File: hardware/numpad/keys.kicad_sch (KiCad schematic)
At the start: 38 parts

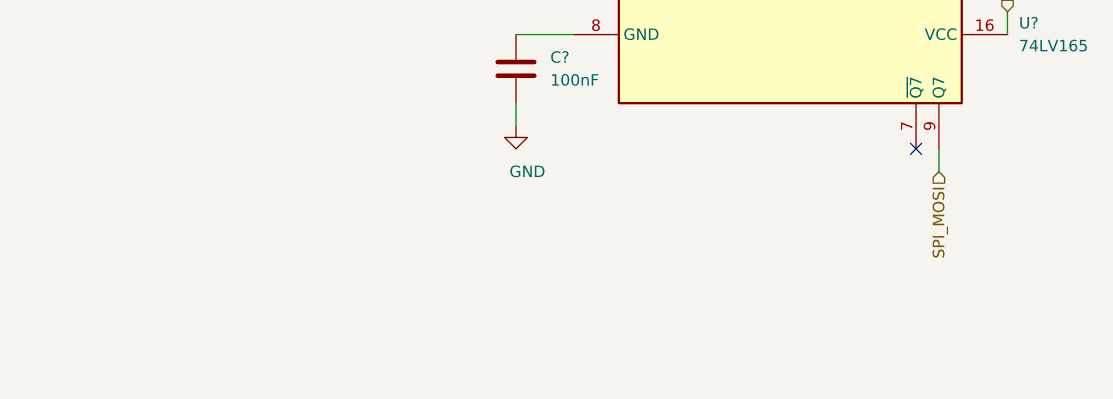
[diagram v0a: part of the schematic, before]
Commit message: Add the missing MISO to the connector
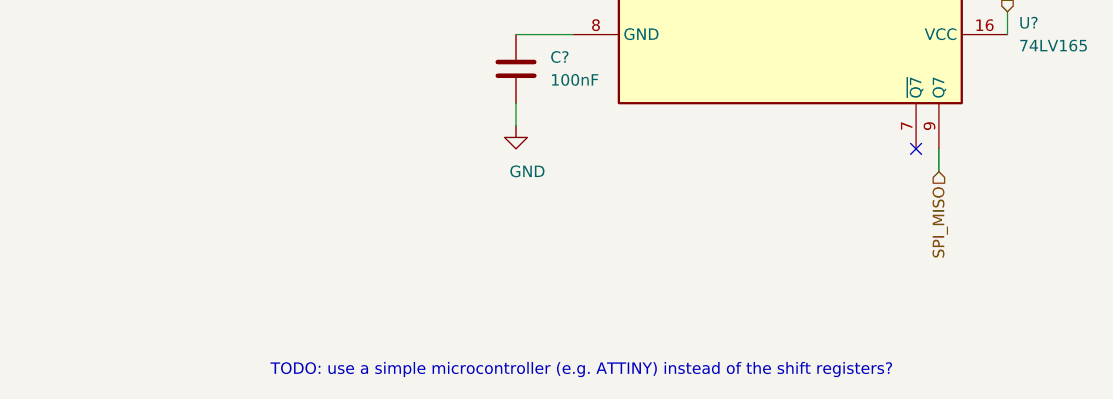
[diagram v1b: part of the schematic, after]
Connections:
- net SPI_MOSI: no longer U?.9 (Q7)
- new net SPI_MISO: U?.9 (Q7)
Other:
- note added: "TODO: use a simple microcontroller (e.g. ATTINY) instead of the shift registers?"
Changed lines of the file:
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@@
   (junction (at 158.75 101.6) (diameter 1.016) (color 0 0 0 0))
   (junction (at 158.75 152.4) (diameter 1.016) (color 0 0 0 0))
+  (no_connect (at 120.65 231.14))
+  (no_connect (at 107.95 205.74))
   (no_connect (at 110.49 205.74))
   (no_connect (at 105.41 205.74))
+  (no_connect (at 123.19 205.74))
   (no_connect (at 67.31 73.66))
-  (no_connect (at 123.19 205.74))
   (no_connect (at 102.87 205.74))
-  (no_connect (at 120.65 231.14))
-  (no_connect (at 107.95 205.74))
   (wire (pts (xy 31.75 55.88) (xy 34.29 55.88))
     (stroke (width 0) (type solid) (color 0 0 0 0))
@@
     (effects (font (size 1.27 1.27)) (justify left bottom))
   )
+  (text "TODO: use a simple microcontroller (e.g. ATTINY) instead of the shift registers?"
+    (at 118.11 256.54 0)
+    (effects (font (size 1.27 1.27)) (justify right bottom))
+  )
   (hierarchical_label "SPI_SCK" (shape input) (at 31.75 55.88 180)
     (effects (font (size 1.27 1.27)) (justify right))
@@
     (effects (font (size 1.27 1.27)) (justify left))
   )
-  (hierarchical_label "SPI_MOSI" (shape input) (at 123.19 233.68 270)
+  (hierarchical_label "SPI_MISO" (shape input) (at 123.19 233.68 270)
     (effects (font (size 1.27 1.27)) (justify right))
   )

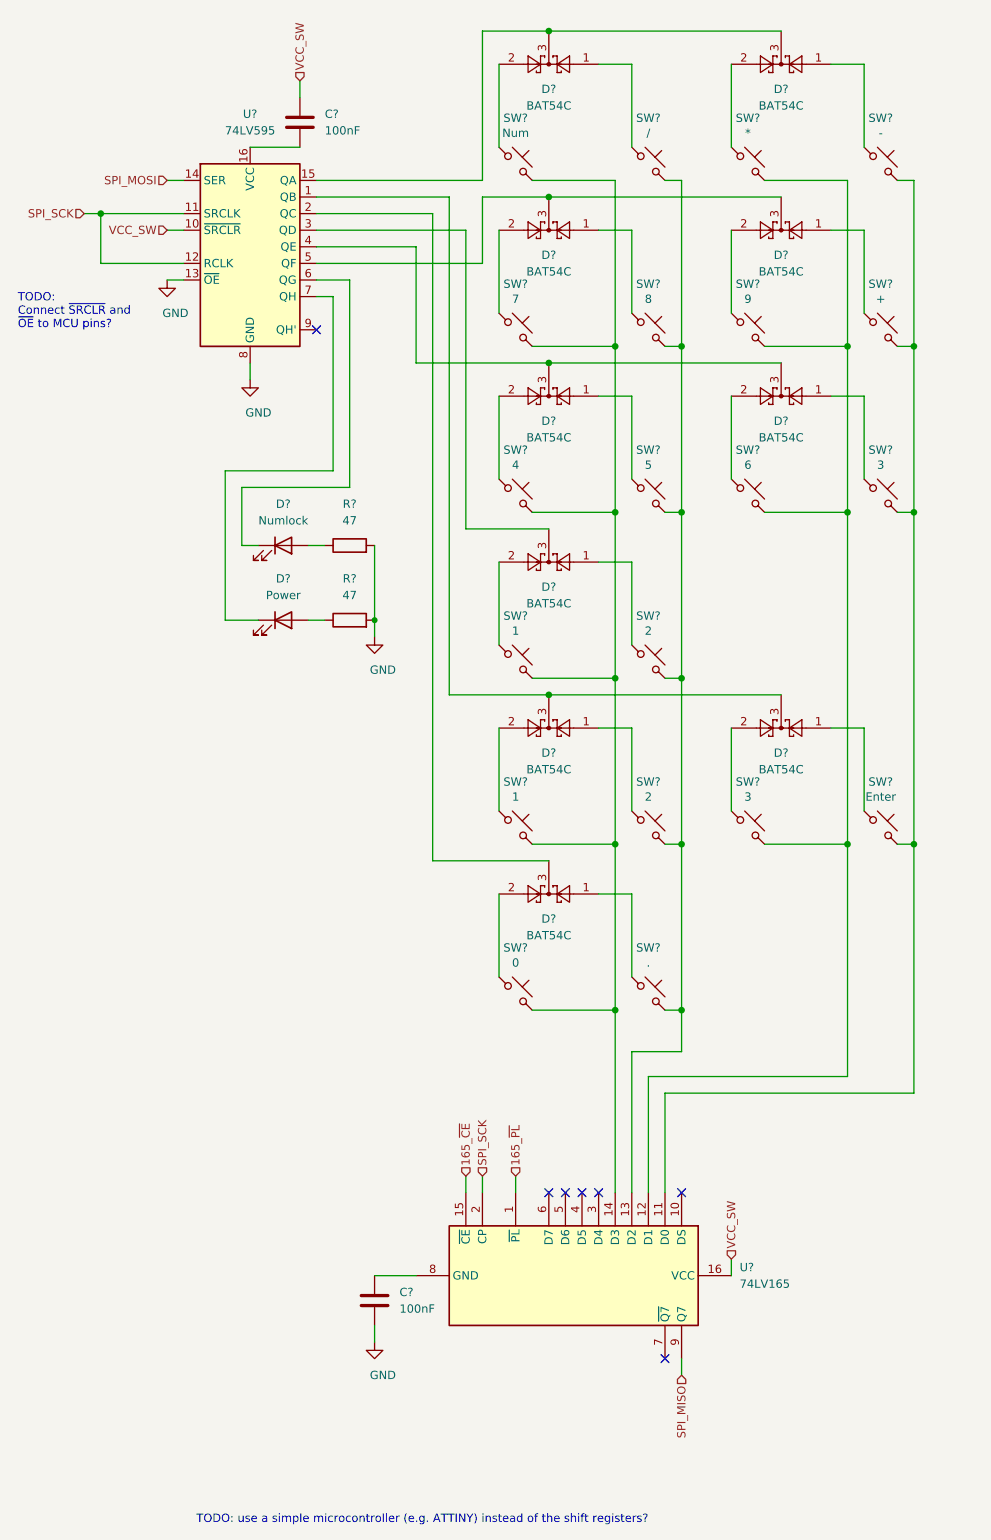
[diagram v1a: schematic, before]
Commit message: WIP: numpad with an ATtiny
As the newer versions of the ATtiny cannot be programmed using an
In-Circuit-Programmer based on SPI this variant is not pursued further.
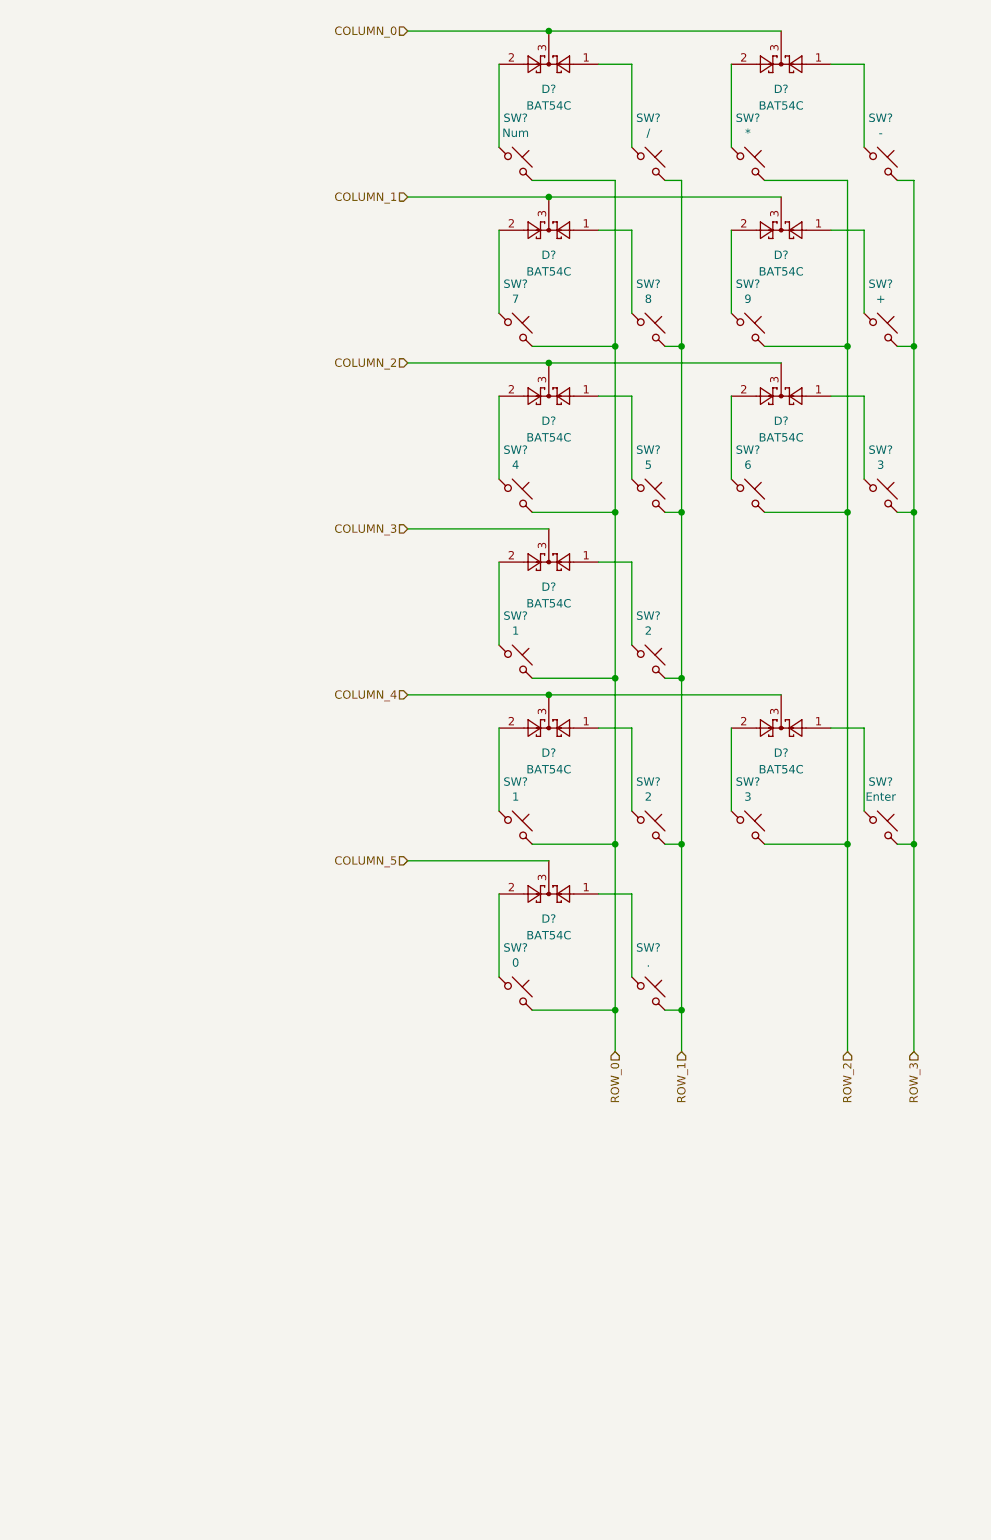
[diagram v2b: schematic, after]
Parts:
- removed C? (x2): 100nF, symbol Device:C
- removed D?: Numlock, symbol Device:LED
- removed D?: Power, symbol Device:LED
- removed R? (x2): 47, symbol Device:R
- removed U?: 74LV595, Package_SO:TSSOP-16_4.4x5mm_P0.65mm, symbol 74xx:74HC595
- removed U?: 74LV165, Package_SO:TSSOP-16_4.4x5mm_P0.65mm, symbol 74xx:74LS165
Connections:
- net ROW_3: now reaches SW?.2, SW?.2, SW?.2, SW?.2
- net ROW_0: now reaches SW?.2, SW?.2, SW?.2, SW?.2, SW?.2, SW?.2
- net COLUMN_0: now reaches D?.3, D?.3
- net COLUMN_2: now reaches D?.3, D?.3
- net COLUMN_3: now reaches D?.3
- net COLUMN_4: now reaches D?.3, D?.3
- net ROW_1: now reaches SW?.2, SW?.2, SW?.2, SW?.2, SW?.2, SW?.2
- net ROW_2: now reaches SW?.2, SW?.2, SW?.2, SW?.2
- net COLUMN_1: now reaches D?.3, D?.3
- net COLUMN_5: now reaches D?.3
- no-connect marks 7 -> 0
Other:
- note removed: "TODO: Connect ~SRCLR and ~OE to MCU pins?"
- note removed: "TODO: use a simple microcontroller (e.g. ATTINY) instead of the shift registers?"

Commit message: Add first rough version of the numpad PCB
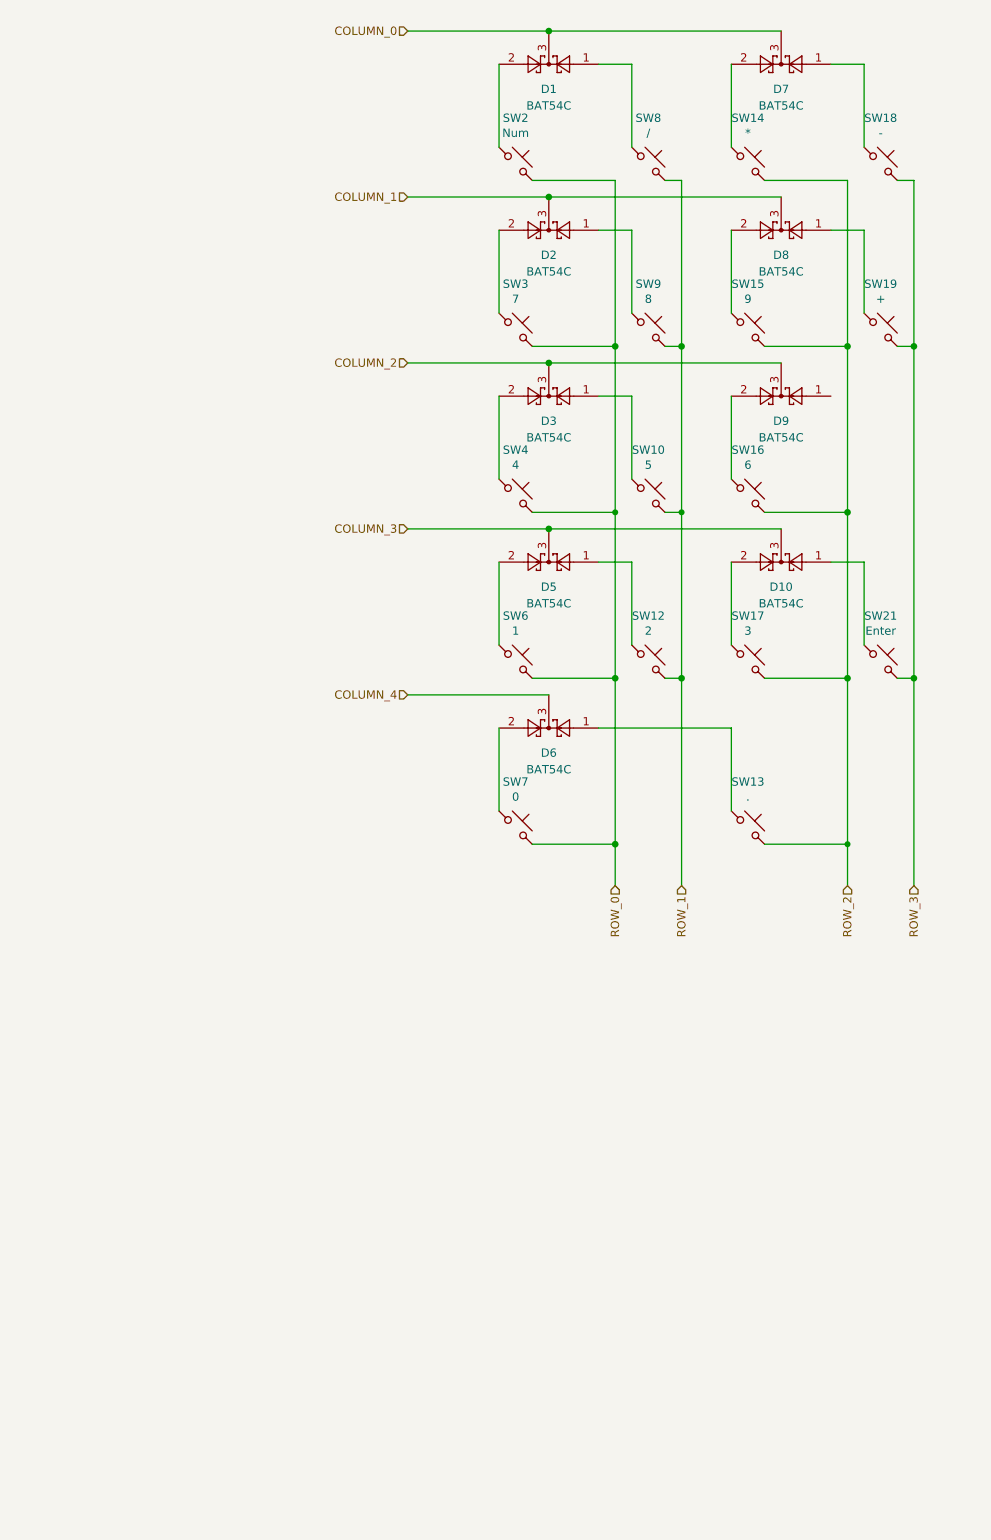
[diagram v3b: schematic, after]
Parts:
- removed D?: BAT54C, Package_TO_SOT_SMD:SOT-23, symbol Diode:BAT54C
- removed SW?: 2, footprints:SW_Cherry_MX_1.00u_PCB, symbol Switch:SW_Push_45deg
- removed SW?: 1, footprints:SW_Cherry_MX_1.75u_PCB, symbol Switch:SW_Push_45deg
- removed SW?: 3, footprints:SW_Cherry_MX_1.00u_PCB, symbol Switch:SW_Push_45deg
- SW13, SW6: renamed from SW?; footprint footprints:SW_Cherry_MX_1.25u_PCB -> footprints:SW_Cherry_MX_1.00u_PCB
- SW19, SW21: renamed from SW?; footprint footprints:SW_Cherry_MX_1.00u_PCB -> footprints:SW_Cherry_MX_2.00u_PCB
- SW4: renamed from SW?; footprint footprints:SW_Cherry_MX_1.50u_PCB -> footprints:SW_Cherry_MX_1.00u_PCB
- SW7: renamed from SW?; footprint footprints:SW_Cherry_MX_1.25u_PCB -> footprints:SW_Cherry_MX_2.00u_PCB
- gave numbers to parts that had none: 20
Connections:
- net COLUMN_5 is gone; now on net COLUMN_4: D6.3
- net COLUMN_3: now also D10.3, D5.3
- net COLUMN_4: no longer D10.3, D5.3
- net ROW_1: no longer SW13.2
- net ROW_2: now also SW13.2
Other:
- moved on the sheet: D10, D5, D6, SW12, SW13, SW17, SW21, SW6, SW7

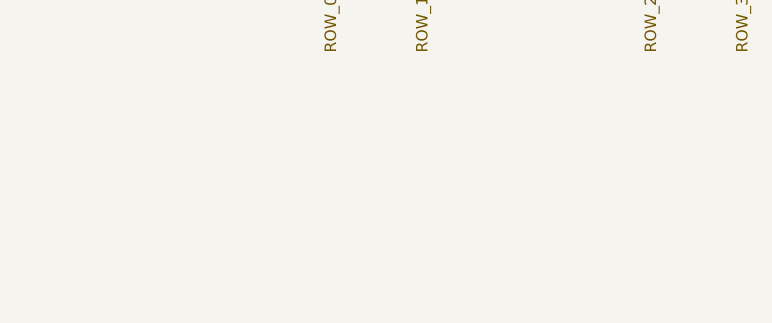
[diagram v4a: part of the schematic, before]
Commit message: Add pull-up resistors to the key matrix
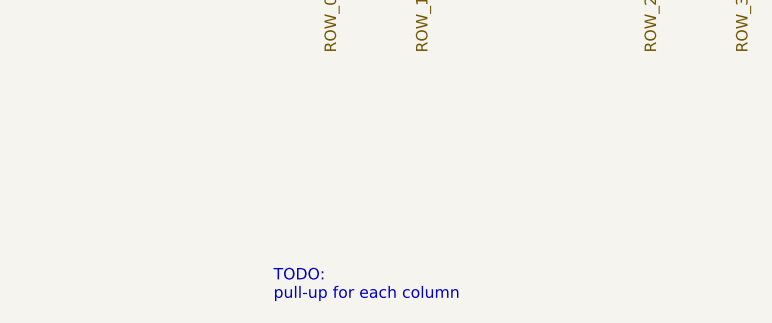
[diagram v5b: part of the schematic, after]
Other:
- note added: "TODO: pull-up for each column"
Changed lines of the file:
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@@
     (stroke (width 0) (type solid) (color 0 0 0 0))
+  )
+  (text "TODO:\npull-up for each column" (at 106.68 194.31 0)
+    (effects (font (size 1.27 1.27)) (justify left bottom))
   )
   (hierarchical_label "COLUMN_0" (shape input) (at 81.28 27.94 180)

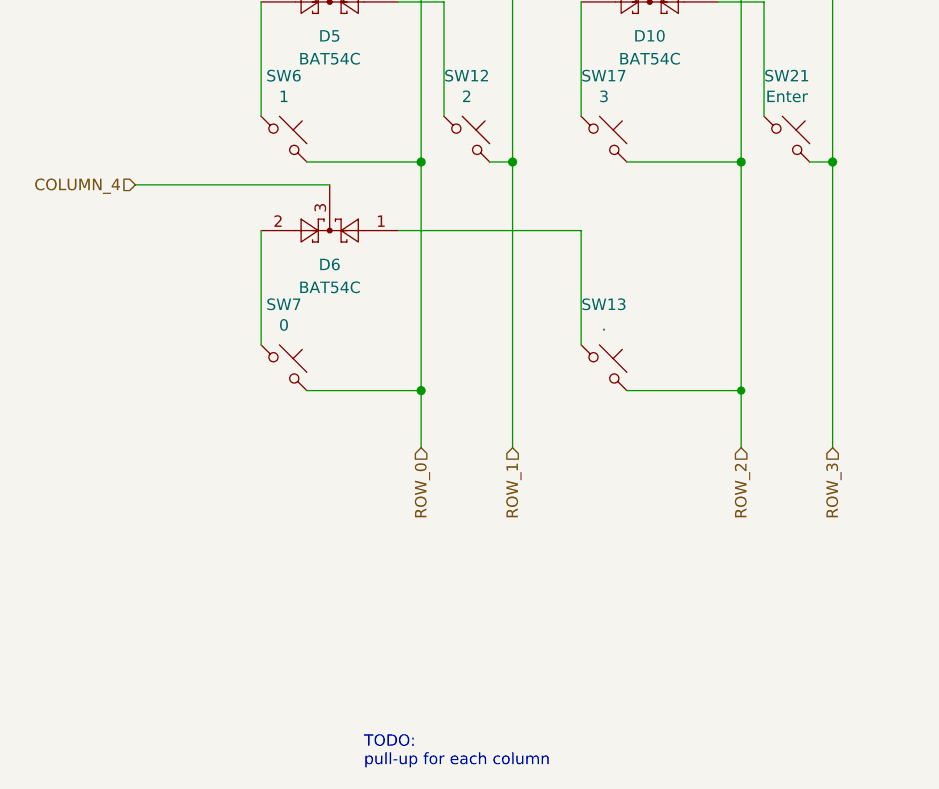
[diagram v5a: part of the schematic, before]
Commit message: Numpad: add pullup resistors to the key matrix
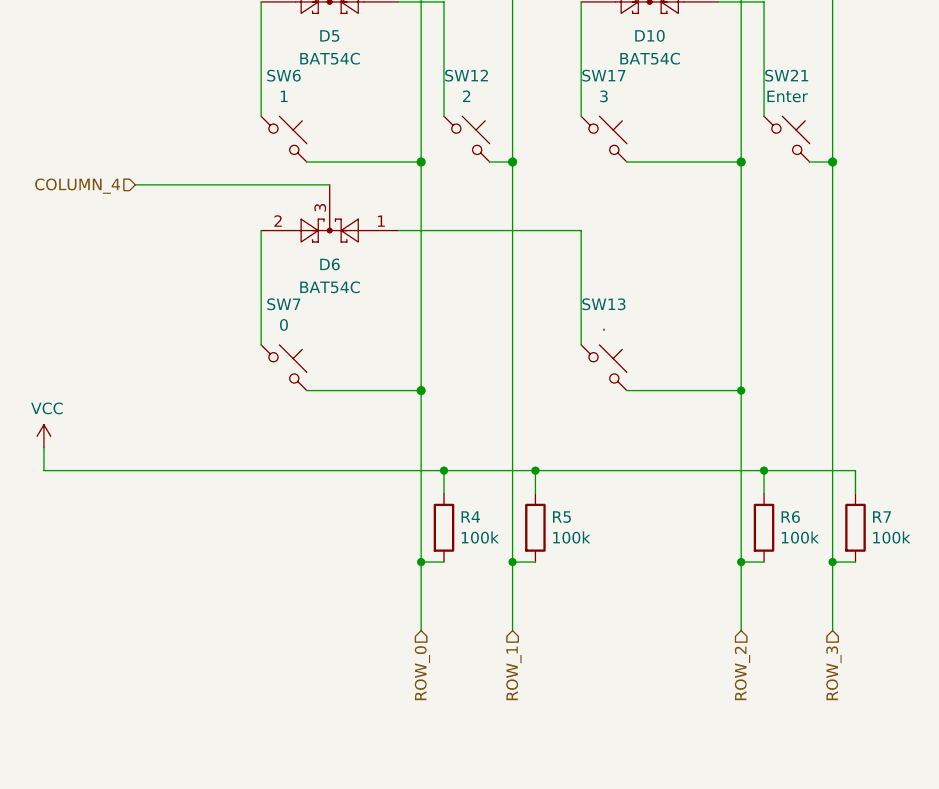
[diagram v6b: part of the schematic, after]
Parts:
- added R4, R5, R6, R7: 100k, Resistor_SMD:R_0603_1608Metric_Pad0.98x0.95mm_HandSolder, symbol Device:R
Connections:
- net ROW_0: now also R4.2
- net ROW_1: now also R5.2
- net ROW_2: now also R6.2
- net ROW_3: now also R7.2
- new net VCC: R4.1, R5.1, R6.1, R7.1
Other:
- note removed: "TODO: pull-up for each column"

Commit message: Numpad: exchange key identifer
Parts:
- SW13: value . -> dot
- SW14: value * -> times
- SW18: value - -> minus
- SW19: value + -> plus
- SW8: value / -> divide
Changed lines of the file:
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@@
     (in_bom yes) (on_board yes)
     (property "Reference" "SW8" (id 0) (at 118.11 41.2558 0))
-    (property "Value" "/" (id 1) (at 118.11 43.555 0))
+    (property "Value" "divide" (id 1) (at 118.11 43.555 0))
     (property "Footprint" "footprints:SW_Cherry_MX_1.00u_PCB" (id 2) (at 118.11 48.26 0)
       (effects (font (size 1.27 1.27)) hide)
@@
     (in_bom yes) (on_board yes)
     (property "Reference" "SW14" (id 0) (at 133.35 41.2558 0))
-    (property "Value" "*" (id 1) (at 133.35 43.555 0))
+    (property "Value" "times" (id 1) (at 133.35 43.555 0))
     (property "Footprint" "footprints:SW_Cherry_MX_1.00u_PCB" (id 2) (at 133.35 48.26 0)
       (effects (font (size 1.27 1.27)) hide)
@@
     (in_bom yes) (on_board yes)
     (property "Reference" "SW13" (id 0) (at 133.35 142.8558 0))
-    (property "Value" "." (id 1) (at 133.35 145.155 0))
+    (property "Value" "dot" (id 1) (at 133.35 145.155 0))
     (property "Footprint" "footprints:SW_Cherry_MX_1.00u_PCB" (id 2) (at 133.35 149.86 0)
       (effects (font (size 1.27 1.27)) hide)
@@
     (in_bom yes) (on_board yes)
     (property "Reference" "SW18" (id 0) (at 153.67 41.2558 0))
-    (property "Value" "-" (id 1) (at 153.67 43.555 0))
+    (property "Value" "minus" (id 1) (at 153.67 43.555 0))
     (property "Footprint" "footprints:SW_Cherry_MX_1.00u_PCB" (id 2) (at 153.67 48.26 0)
       (effects (font (size 1.27 1.27)) hide)
@@
     (in_bom yes) (on_board yes)
     (property "Reference" "SW19" (id 0) (at 153.67 66.6558 0))
-    (property "Value" "+" (id 1) (at 153.67 68.955 0))
+    (property "Value" "plus" (id 1) (at 153.67 68.955 0))
     (property "Footprint" "footprints:SW_Cherry_MX_2.00u_PCB" (id 2) (at 153.67 73.66 0)
       (effects (font (size 1.27 1.27)) hide)

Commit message: Numpad: WIP: design PCB
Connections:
- no-connect marks 0 -> 1
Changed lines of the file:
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@@
   (junction (at 158.75 127) (diameter 1.016) (color 0 0 0 0))
   (junction (at 158.75 171.45) (diameter 0.9144) (color 0 0 0 0))
+  (no_connect (at 146.05 83.82))
   (wire (pts (xy 71.12 161.29) (xy 71.12 158.75))
     (stroke (width 0) (type solid) (color 0 0 0 0))
